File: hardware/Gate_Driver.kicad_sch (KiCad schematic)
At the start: 30 parts, among them U1 DRV8323RSRGZR

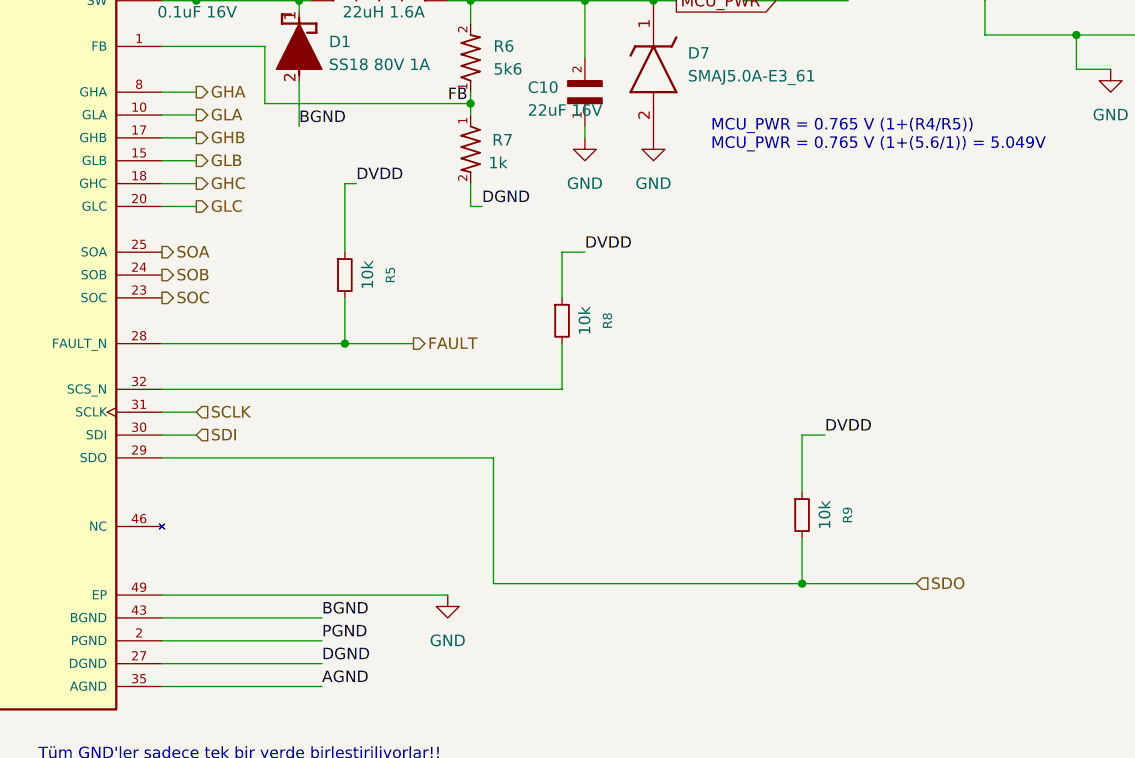
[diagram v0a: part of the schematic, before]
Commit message: After graduation presantition. USB differantial ways improved for usb connection issue. DRV83233 Enable and nSCS pins changed to be in true connection with STM32G431. ETC
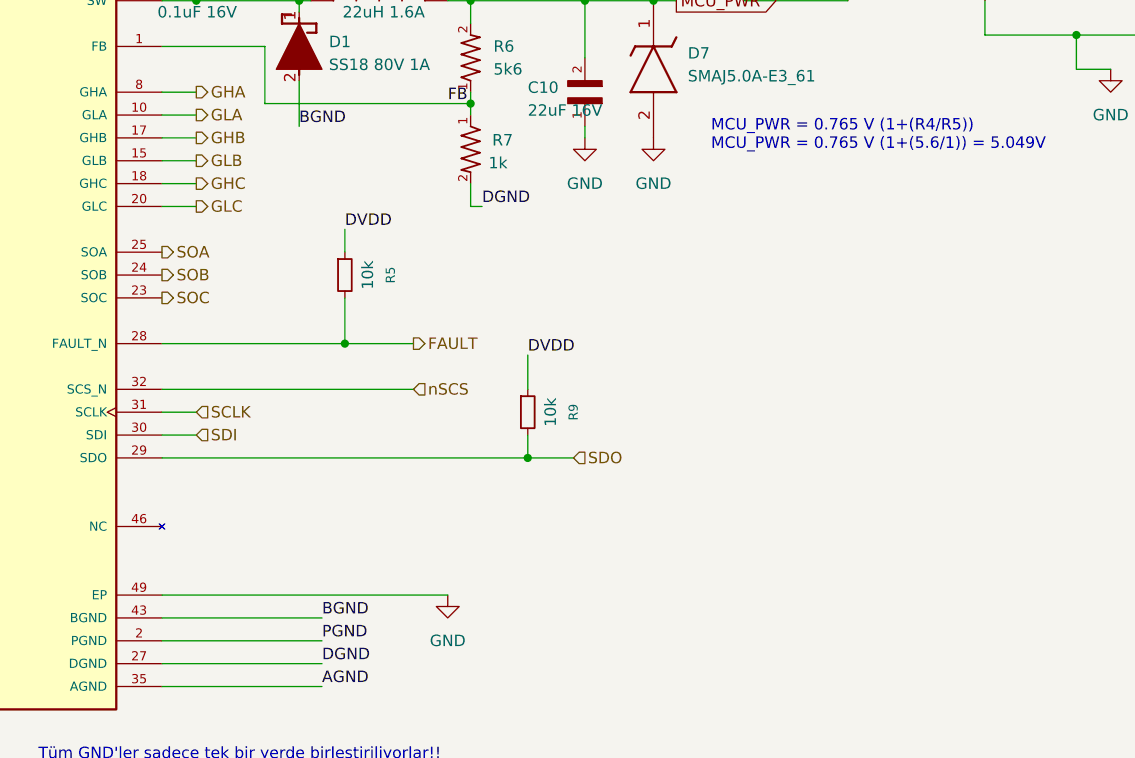
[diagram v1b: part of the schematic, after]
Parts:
- removed R8: 10k, Resistor_SMD:R_0603_1608Metric_Pad0.98x0.95mm_HandSolder, symbol Device:R_Small
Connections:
- net nSCS: now reaches U1.32 (SCS_N)
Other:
- moved on the sheet: R9
